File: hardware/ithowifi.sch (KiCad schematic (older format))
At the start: 6 parts, among them J1 conn

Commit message: Updated PCB to version 1.1, added more advanced firmware - PCB version 1.0 wasn't working properly, updated version 1.1 is tested and works - Uploaded a more advanced, 'field' configurable firmware and OTA support - Added images of the add-on - Updated readme
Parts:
- removed ESP8266_NodeMCU_v2: U1, ESP12E_DEVKIT, symbol MCU_NodeMCU:ESP12E_DEVKIT
- removed ISO1540: U3, Package_SO:SOIC-8_3.9x4.9mm_P1.27mm, symbol Isolator:ISO1540
- added D1: LED, LED_SMD:LED_1206_3216Metric, symbol Device:LED
- added Q1, Q2: BSS138, Package_TO_SOT_SMD:SOT-23, symbol Transistor_FET:BSS138
- added R_SDA2, R_SDA3: R4.7K, Resistor_SMD:R_1206_3216Metric, symbol Device:R
- added R_SDA4: R100, Resistor_SMD:R_1206_3216Metric, symbol Device:R
- added U1: WeMos_mini, wemos_d1_mini:D1_mini_board, symbol wemos_mini:WeMos_mini
- R_SCL1, R_SDA1: footprint Resistor_THT:R_Axial_DIN0309_L9.0mm_D3.2mm_P2.54mm_Vertical -> Resistor_SMD:R_1206_3216Metric
- renumbered R-78E5.0-1.0 to R-78E5.0-1.1
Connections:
- wire segments 55 -> 50
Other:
- moved on the sheet: R_SCL1, R_SDA1

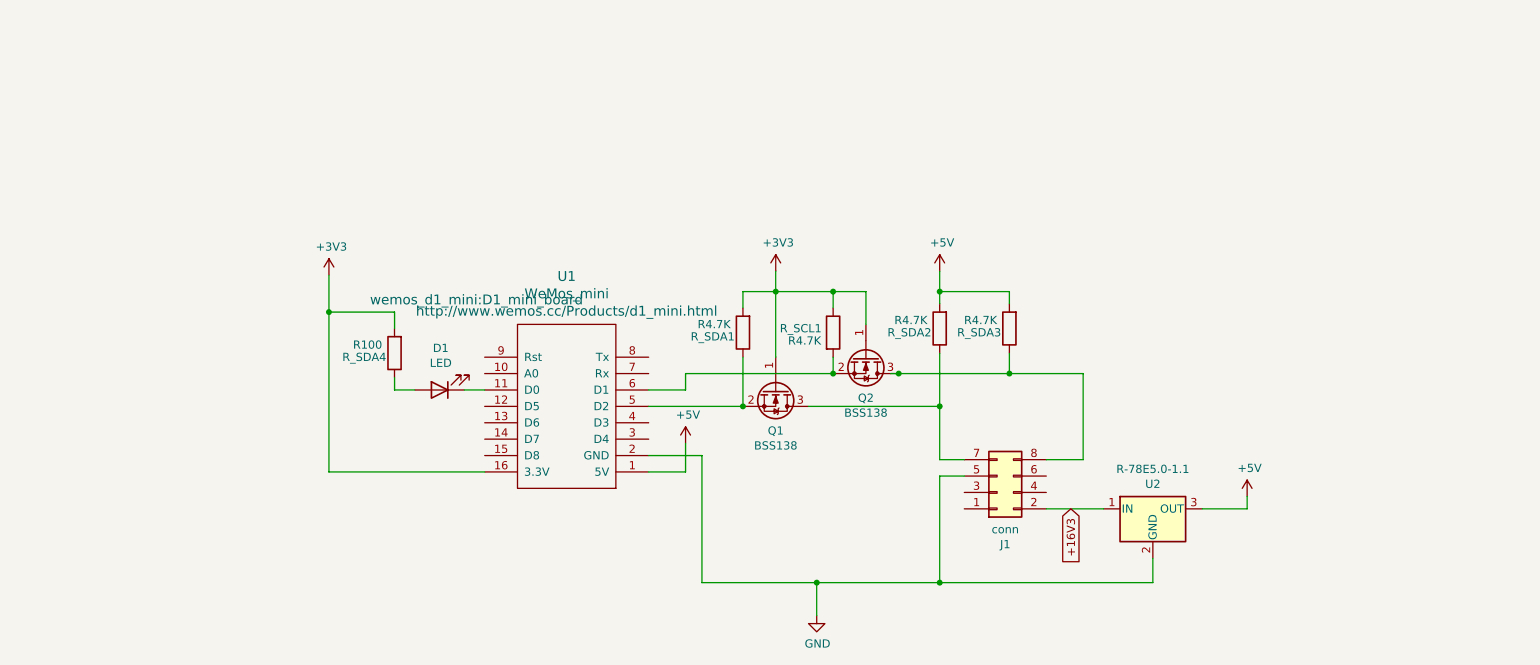
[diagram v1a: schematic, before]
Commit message: Release 1.2
- Updated PCB design to accommodate a ATTiny 1614 to handle the I2C init with the itho box (Wemos often boots too slow to handle this reliable)
- Added firmware for the ATTiny
- Updated Wemos and basic firmware to work with the ATTiny 1614
- Improved WiFi stability
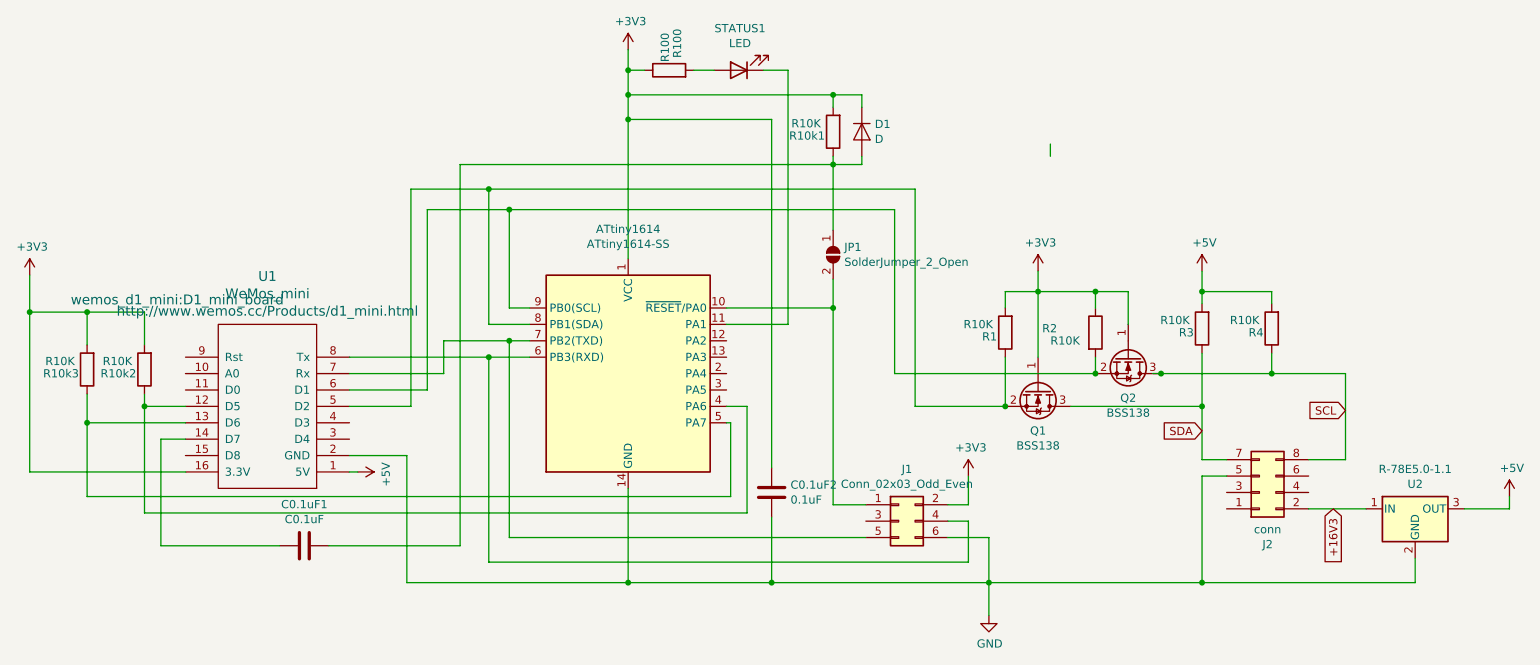
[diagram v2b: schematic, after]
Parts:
- added ATtiny1614: ATtiny1614-SS, Package_SO:SOIC-14_3.9x8.7mm_P1.27mm, symbol MCU_Microchip_ATtiny:ATtiny1614-SS
- added C0.1uF1: C0.1uF, Inductor_SMD:L_1206_3216Metric, symbol Device:C
- added C0.1uF2: 0.1uF, Inductor_SMD:L_1206_3216Metric, symbol Device:C
- added D1: D, Diode_SMD:D_SOD-123, symbol Device:D
- added J1: Conn_02x03_Odd_Even, Connector_PinHeader_2.54mm:PinHeader_2x03_P2.54mm_Vertical_SMD, symbol Connector_Generic:Conn_02x03_Odd_Even
- added JP1: SolderJumper_2_Open, Jumper:SolderJumper-2_P1.3mm_Open_RoundedPad1.0x1.5mm, symbol Jumper:SolderJumper_2_Open
- added R10k1, R10k2, R10k3: R10K, Resistor_SMD:R_1206_3216Metric, symbol Device:R
- Q1, Q2: footprint Package_TO_SOT_SMD:SOT-23 -> Package_TO_SOT_SMD:SOT-23W
- R1: renamed from R_SDA1; value R4.7K -> R10K
- R2: renamed from R_SCL1; value R4.7K -> R10K
- R3: renamed from R_SDA2; value R4.7K -> R10K
- R4: renamed from R_SDA3; value R4.7K -> R10K
- renumbered J1 to J2, R_SDA4 to R100, D1 to STATUS1
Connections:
- net labels added: SCL, SDA
- wire segments 50 -> 122
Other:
- moved on the sheet: J2, Q1, Q2, R-78E5.0-1.1, R1, R100, R2, R3, R4, STATUS1, U1

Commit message: Test v2.0
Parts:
- removed C0.1uF1: C0.1uF, Inductor_SMD:L_1206_3216Metric, symbol Device:C
- removed D1: D, Diode_SMD:D_SOD-123, symbol Device:D
- removed JP1: SolderJumper_2_Open, Jumper:SolderJumper-2_P1.3mm_Open_RoundedPad1.0x1.5mm, symbol Jumper:SolderJumper_2_Open
- removed R10k1, R10k3: R10K, Resistor_SMD:R_1206_3216Metric, symbol Device:R
- added J3: Conn_Coaxial, Connector_Coaxial:SMA_Amphenol_132289_EdgeMount, symbol Connector:Conn_Coaxial
- added U2: CC1101-868MHz-Module, nrg_watch:CC1101-868MHz-Module, symbol nrg_watch:CC1101-868MHz-Module
- C1: renamed from C0.1uF2; value 0.1uF -> 0,1uF; footprint Inductor_SMD:L_1206_3216Metric -> Inductor_SMD:L_0805_2012Metric
- Q1, Q2: footprint Package_TO_SOT_SMD:SOT-23W -> Package_TO_SOT_SMD:SOT-23
- R1, R2, R3, R4: footprint Resistor_SMD:R_1206_3216Metric -> Resistor_SMD:R_0805_2012Metric
- R5: renamed from R100; footprint Resistor_SMD:R_1206_3216Metric -> Resistor_SMD:R_0805_2012Metric
- R6: renamed from R10k2; footprint Resistor_SMD:R_1206_3216Metric -> Resistor_SMD:R_0805_2012Metric
- STATUS1: footprint LED_SMD:LED_1206_3216Metric -> LED_SMD:LED_0805_2012Metric
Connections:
- net labels added: CLK, CS, IRQ, MISO, MOSI
- wire segments 122 -> 118
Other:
- moved on the sheet: R6

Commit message: Revert "Test v2.0"
This reverts commit 51a6d60645f7c24e24572af265a76d84da59fee7.
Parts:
- removed J3: Conn_Coaxial, Connector_Coaxial:SMA_Amphenol_132289_EdgeMount, symbol Connector:Conn_Coaxial
- removed U2: CC1101-868MHz-Module, nrg_watch:CC1101-868MHz-Module, symbol nrg_watch:CC1101-868MHz-Module
- added C0.1uF1: C0.1uF, Inductor_SMD:L_1206_3216Metric, symbol Device:C
- added D1: D, Diode_SMD:D_SOD-123, symbol Device:D
- added JP1: SolderJumper_2_Open, Jumper:SolderJumper-2_P1.3mm_Open_RoundedPad1.0x1.5mm, symbol Jumper:SolderJumper_2_Open
- added R10k1, R10k3: R10K, Resistor_SMD:R_1206_3216Metric, symbol Device:R
- C0.1uF2: renamed from C1; value 0,1uF -> 0.1uF; footprint Inductor_SMD:L_0805_2012Metric -> Inductor_SMD:L_1206_3216Metric
- Q1, Q2: footprint Package_TO_SOT_SMD:SOT-23 -> Package_TO_SOT_SMD:SOT-23W
- R1, R2, R3, R4: footprint Resistor_SMD:R_0805_2012Metric -> Resistor_SMD:R_1206_3216Metric
- R100: renamed from R5; footprint Resistor_SMD:R_0805_2012Metric -> Resistor_SMD:R_1206_3216Metric
- R10k2: renamed from R6; footprint Resistor_SMD:R_0805_2012Metric -> Resistor_SMD:R_1206_3216Metric
- STATUS1: footprint LED_SMD:LED_0805_2012Metric -> LED_SMD:LED_1206_3216Metric
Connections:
- net labels removed: CLK, CS, IRQ, MISO, MOSI
- wire segments 118 -> 122
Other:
- moved on the sheet: R10k2

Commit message: Version 2.0.3
- Support for hardware revision 2
- Experimental itho RF remote support
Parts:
- removed C0.1uF1: C0.1uF, Inductor_SMD:L_1206_3216Metric, symbol Device:C
- removed D1: D, Diode_SMD:D_SOD-123, symbol Device:D
- removed J1: Conn_02x03_Odd_Even, Connector_PinHeader_2.54mm:PinHeader_2x03_P2.54mm_Vertical_SMD, symbol Connector_Generic:Conn_02x03_Odd_Even
- removed JP1: SolderJumper_2_Open, Jumper:SolderJumper-2_P1.3mm_Open_RoundedPad1.0x1.5mm, symbol Jumper:SolderJumper_2_Open
- removed R10k1, R10k3: R10K, Resistor_SMD:R_1206_3216Metric, symbol Device:R
- removed U1: WeMos_mini, wemos_d1_mini:D1_mini_board, symbol wemos_mini:WeMos_mini
- added C2: 1uF, Capacitor_SMD:C_0805_2012Metric, symbol Device:C
- added C4, C6: 10uF, Capacitor_Tantalum_SMD:CP_EIA-3216-12_Kemet-S, symbol Device:CP
- added C5: 0.1uF, Capacitor_SMD:C_0805_2012Metric, symbol Device:C
- added D1: D_Zener, Diode_SMD:D_SOD-123, symbol Device:D_Zener
- added H1: MountingHole, MountingHole:MountingHole_2.5mm, symbol Mechanical:MountingHole
- added J1: CONN_01X07, Connector_PinHeader_2.54mm:PinHeader_1x07_P2.54mm_Vertical, symbol Connector_Generic:Conn_01x07
- added J3: Conn_Coaxial, Connector_Coaxial:SMA_Amphenol_132289_EdgeMount, symbol Connector:Conn_Coaxial
- added J4: Conn_01x04, Connector_PinHeader_2.54mm:PinHeader_1x04_P2.54mm_Vertical, symbol Connector_Generic:Conn_01x04
- added JP1: Failsafe, Jumper:SolderJumper-2_P1.3mm_Open_RoundedPad1.0x1.5mm, symbol Device:Jumper
- added R10, R7, R8: 10K, Resistor_SMD:R_0805_2012Metric, symbol Device:R
- added R9: R100, Resistor_SMD:R_0805_2012Metric, symbol Device:R
- added U1: ESP32-WROOM, RF_Module:ESP32-WROOM-32, symbol nrg_watch:ESP32-WROOM
- added U2: CC1101-868MHz-Module, nrg_watch:CC1101-868MHz-Module, symbol nrg_watch:CC1101-868MHz-Module
- added U3: AMS1117-3.3, Package_TO_SOT_SMD:SOT-223-3_TabPin2, symbol Regulator_Linear:AMS1117-3.3
- added WIFI_STATUS1: LED, LED_SMD:LED_0805_2012Metric, symbol Device:LED
- ATtiny1614: symbol MCU_Microchip_ATtiny:ATtiny1614-SS -> ithowifi-rescue:ATtiny1614-SS-MCU_Microchip_ATtiny
- C1: renamed from C0.1uF2; value 0.1uF -> 0,1uF; footprint Inductor_SMD:L_1206_3216Metric -> Inductor_SMD:L_0805_2012Metric
- ITHO_STATUS1: renamed from STATUS1; footprint LED_SMD:LED_1206_3216Metric -> LED_SMD:LED_0805_2012Metric
- Q1, Q2: footprint Package_TO_SOT_SMD:SOT-23W -> Package_TO_SOT_SMD:SOT-23
- R1, R2, R3, R4: footprint Resistor_SMD:R_1206_3216Metric -> Resistor_SMD:R_0805_2012Metric
- R5: renamed from R100; footprint Resistor_SMD:R_1206_3216Metric -> Resistor_SMD:R_0805_2012Metric
- R6: renamed from R10k2; footprint Resistor_SMD:R_1206_3216Metric -> Resistor_SMD:R_0805_2012Metric
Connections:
- net labels added: D0, D0/RX0, D1/TX0, D18_SCK, D19_MISO, D23_MOSI, D4_IRQ, D5_SS, EN, UPDI
- wire segments 122 -> 165
- no-connect marks 0 -> 1
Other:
- moved on the sheet: ATtiny1614, C1, ITHO_STATUS1, J2, Q1, Q2, R-78E5.0-1.1, R1, R2, R3, R4, R5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
